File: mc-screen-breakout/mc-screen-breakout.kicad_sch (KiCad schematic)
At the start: 1 part, among them U1 E73-2G4M08S1C

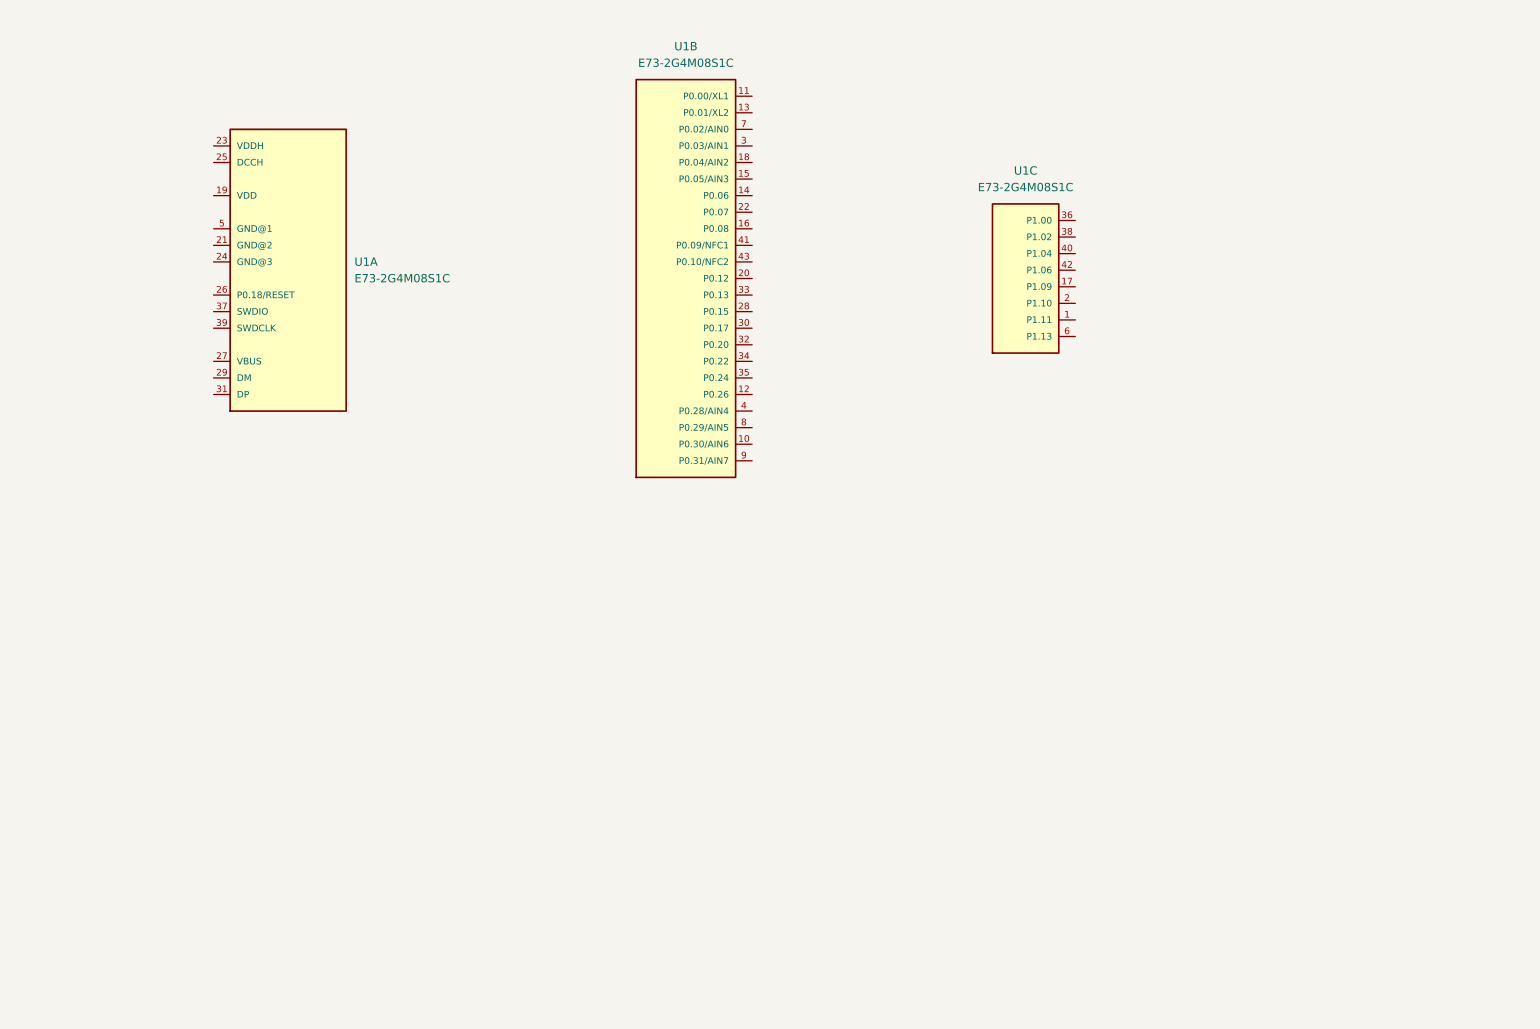
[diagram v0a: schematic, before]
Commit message: Initial microcontroller power on breakout
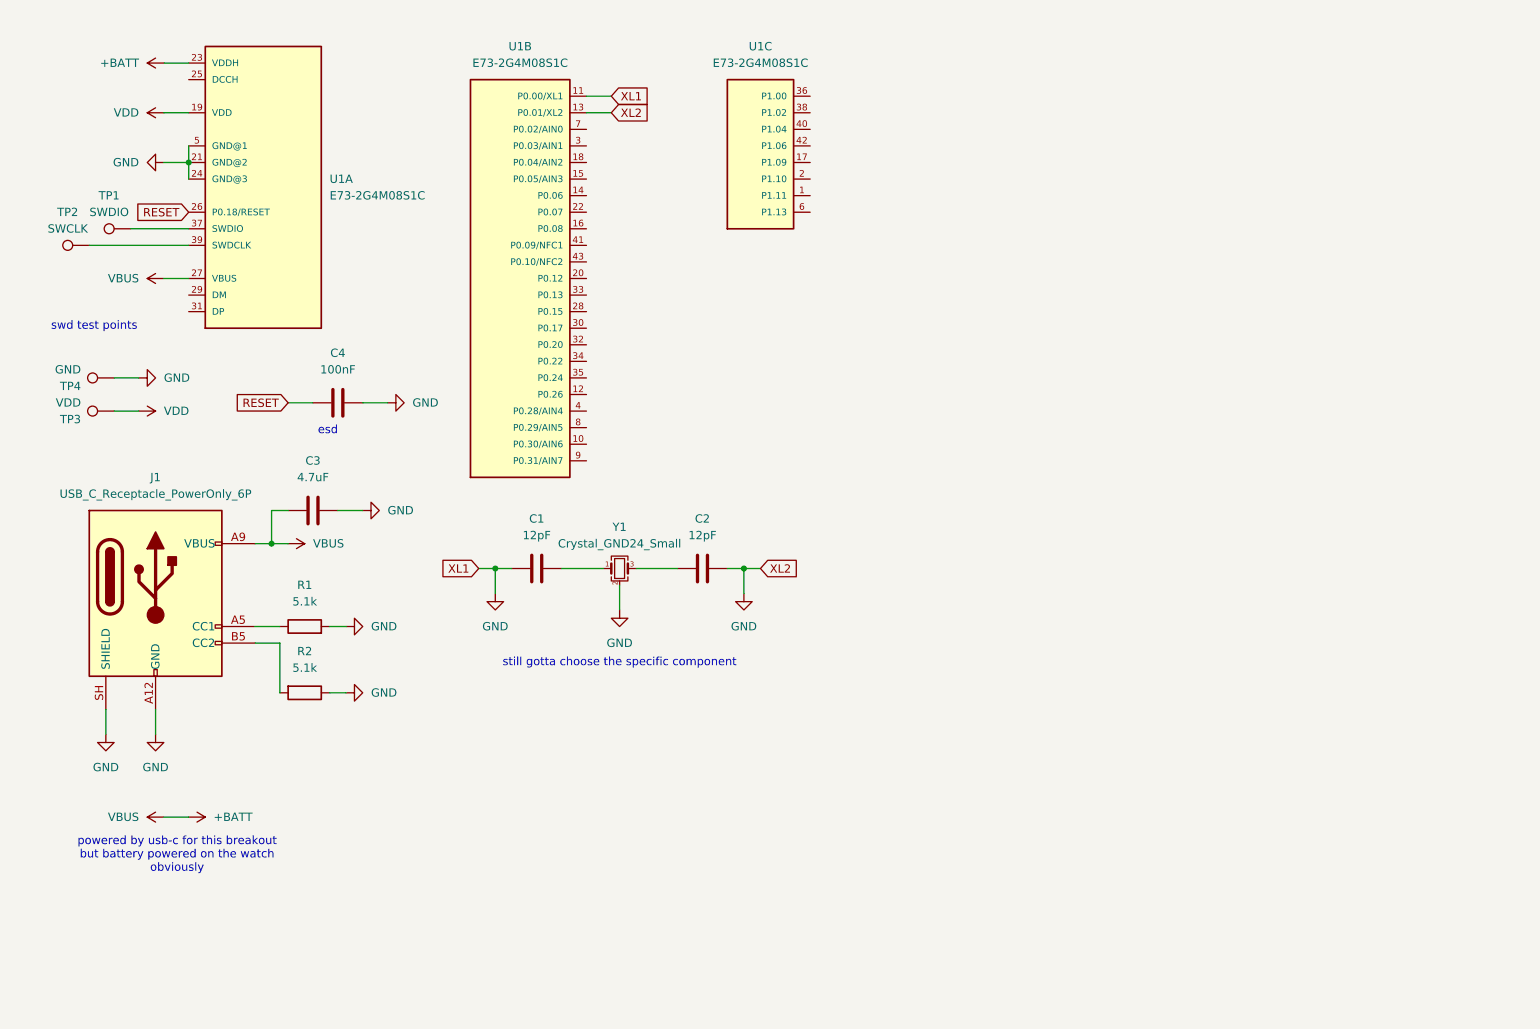
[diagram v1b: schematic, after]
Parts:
- added C1, C2: 12pF, symbol Device:C
- added C3: 4.7uF, symbol Device:C
- added C4: 100nF, symbol Device:C
- added J1: USB_C_Receptacle_PowerOnly_6P, symbol Connector:USB_C_Receptacle_PowerOnly_6P
- added R1, R2: 5.1k, symbol Device:R
- added TP1: SWDIO, symbol Connector:TestPoint
- added TP2: SWCLK, symbol Connector:TestPoint
- added TP3: VDD, symbol Connector:TestPoint
- added TP4: GND, symbol Connector:TestPoint
- added Y1: Crystal_GND24_Small, symbol Device:Crystal_GND24_Small
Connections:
- net GND: now reaches U1.11 (P0.00/XL1)
- net GND: now also U1.13 (P0.01/XL2), U1.21 (GND@2), U1.24 (GND@3), U1.5 (GND@1), C1.1, C2.2, C3.2, C4.2, J1.A12 (GND), J1.B12 (GND), J1.SH (SHIELD), R1.2, R2.1, TP4.1, Y1.2 (G), Y1.4 (G)
- net VDD: now reaches U1.19 (VDD)
- net VDD: now also TP3.1
- net +BATT: now reaches U1.23 (VDDH)
- net +BATT: now also U1.27 (VBUS), C3.1, J1.A9 (VBUS), J1.B9 (VBUS)
- net RESET: now reaches U1.26 (P0.18/RESET)
- net RESET: now also C4.1
- net at U1.37 (SWDIO): now also TP1.1
- net at U1.39 (SWDCLK): now also TP2.1
- new net: J1.A5 (CC1), R1.1
- new net: C1.2, Y1.1
- new net: C2.1, Y1.3
- new net: J1.B5 (CC2), R2.2
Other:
- note added: "esd"
- note added: "powered by usb-c for this breakout but battery powered on the watch obviously"
- note added: "still gotta choose the specific component"
- note added: "swd test points"
- moved on the sheet: U1A, U1B, U1C

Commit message: Switched to new Raytac module
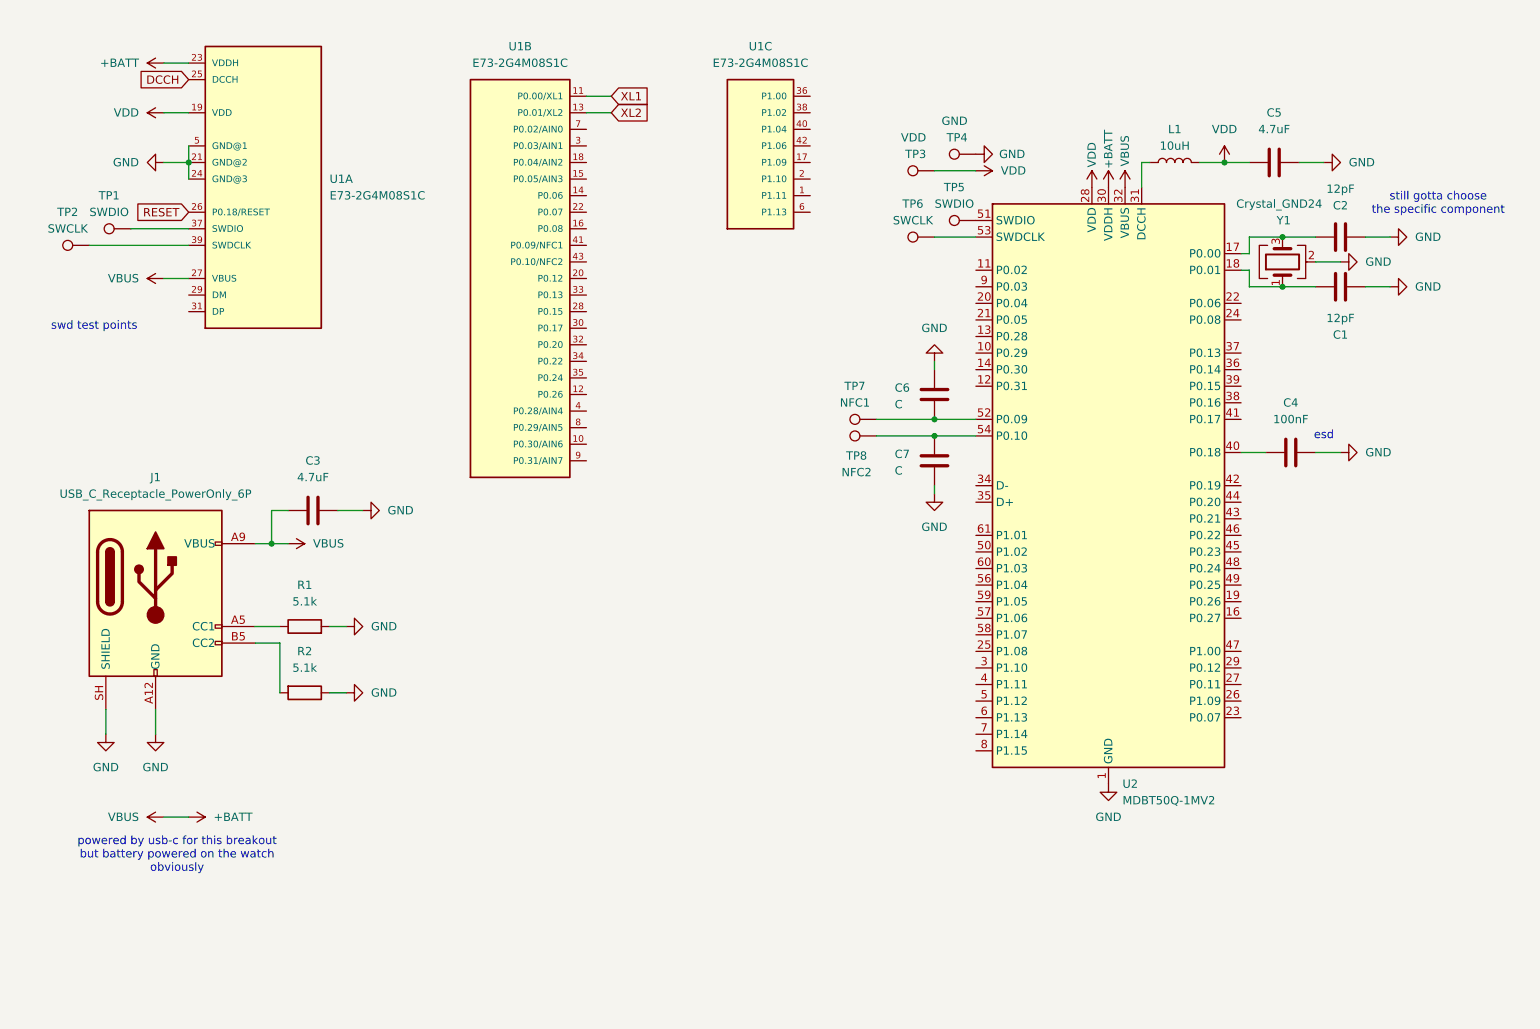
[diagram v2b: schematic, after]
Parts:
- removed Y1: Crystal_GND24_Small, symbol Device:Crystal_GND24_Small
- added C5: 4.7uF, symbol Device:C
- added C6, C7: C, symbol Device:C
- added L1: 10uH, symbol Device:L
- added TP5: SWDIO, symbol Connector:TestPoint
- added TP6: SWCLK, symbol Connector:TestPoint
- added TP7: NFC1, symbol Connector:TestPoint
- added TP8: NFC2, symbol Connector:TestPoint
- added U2: MDBT50Q-1MV2, RF_Module:Raytac_MDBT50Q, symbol RF_Module:MDBT50Q-1MV2
- added Y1: Crystal_GND24, symbol Device:Crystal_GND24
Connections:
- net +BATT: now also U2.30 (VDDH), U2.32 (VBUS)
- net GND: now also C5.2, C6.1, C7.2, U2.1 (GND), U2.15 (GND), U2.2 (GND), U2.33 (GND), U2.55 (GND), Y1.2 (G), Y1.4 (G); no longer U1.11 (P0.00/XL1), U1.13 (P0.01/XL2)
- net RESET: no longer C4.1
- net VDD: now also C5.1, L1.2, U2.28 (VDD)
- net at C1.2: now also U2.18 (P0.01), Y1.1
- net at C2.1: now also U2.17 (P0.00), Y1.3
- net DCCH: now reaches U1.25 (DCCH)
- new net: L1.1, U2.31 (DCCH)
- new net: C4.1, U2.40 (P0.18)
- new net: TP6.1, U2.53 (SWDCLK)
- new net: C7.1, TP8.1, U2.54 (P0.10)
- new net: C6.2, TP7.1, U2.52 (P0.09)
- new net: TP5.1, U2.51 (SWDIO)
- new net XL1: U1.11 (P0.00/XL1)
- new net XL2: U1.13 (P0.01/XL2)
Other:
- moved on the sheet: C4, TP3, TP4

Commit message: Added LCD FPC female connector
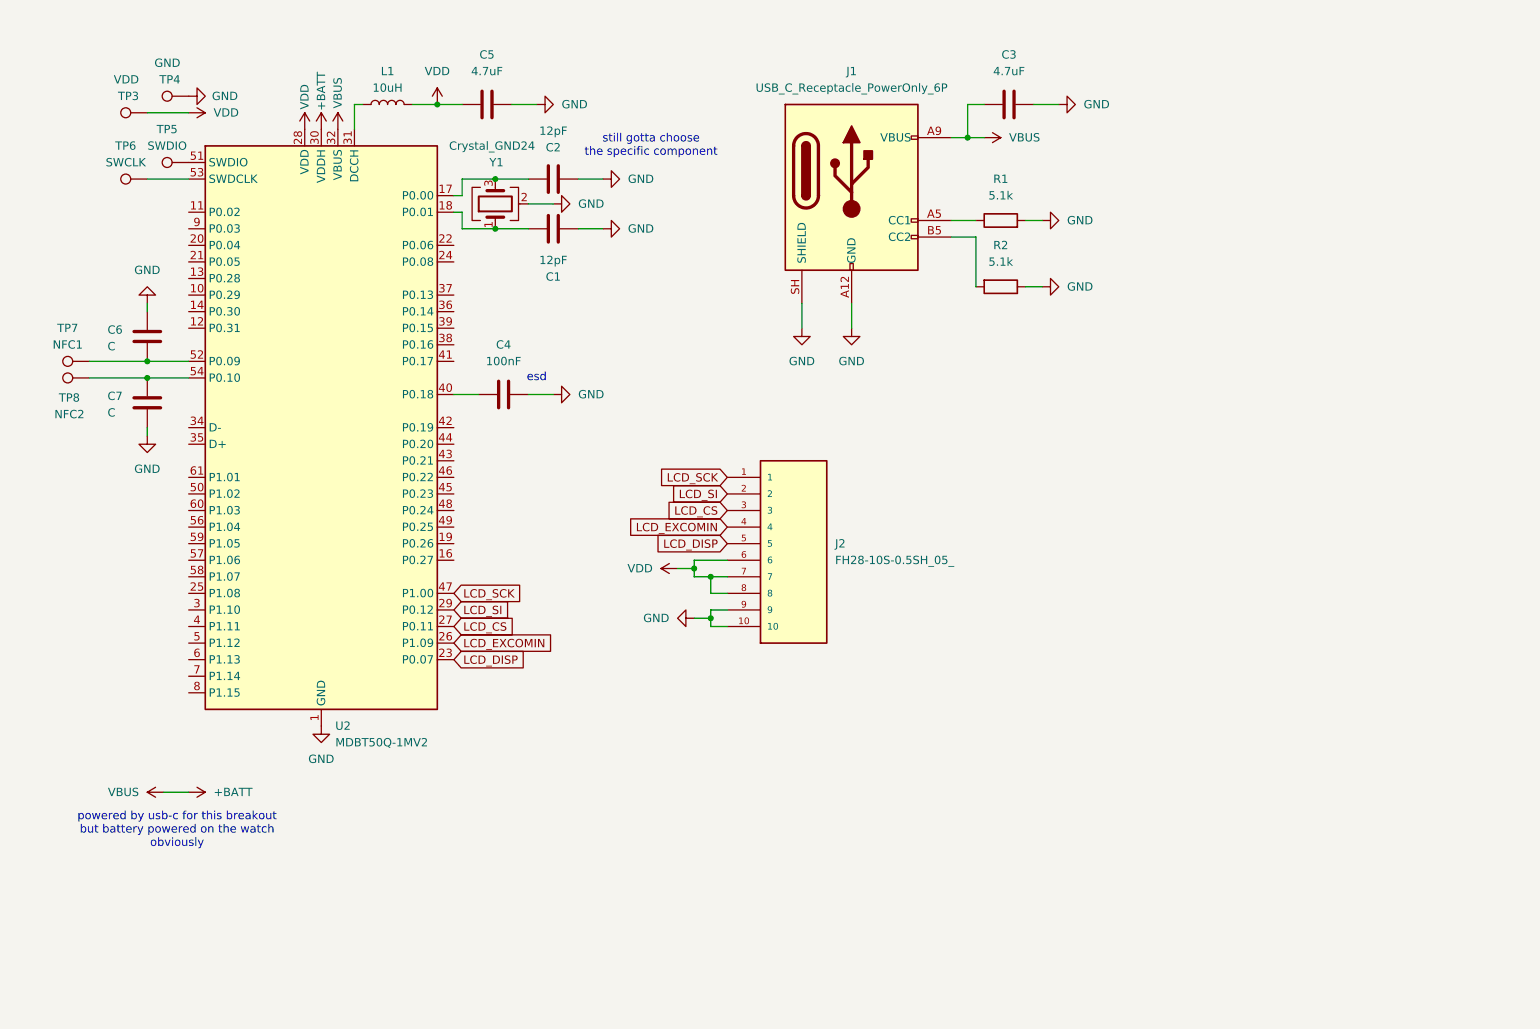
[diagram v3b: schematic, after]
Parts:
- removed TP1: SWDIO, symbol Connector:TestPoint
- removed TP2: SWCLK, symbol Connector:TestPoint
- removed U1: E73-2G4M08S1C, E73-2G4M08S1C:E73-2G4M08S1C, symbol E73-2G4M08S1C:E73-2G4M08S1C
- added J2: FH28-10S-0.5SH_05_, FH28-10S-0.5SH_05_:HIROSE_FH28-10S-0.5SH_05_, symbol FH28-10S-0.5SH_05_:FH28-10S-0.5SH_05_
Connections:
- net GND: now also J2.10, J2.9
- net VDD: now also J2.6, J2.7, J2.8
- net LCD_DISP: now reaches U2.23 (P0.07)
- net LCD_DISP: now also J2.5
- net LCD_EXCOMIN: now reaches U2.26 (P1.09)
- net LCD_EXCOMIN: now also J2.4
- net LCD_CS: now reaches U2.27 (P0.11)
- net LCD_CS: now also J2.3
- net LCD_SI: now reaches U2.29 (P0.12)
- net LCD_SI: now also J2.2
- net LCD_SCK: now reaches U2.47 (P1.00)
- net LCD_SCK: now also J2.1
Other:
- note removed: "swd test points"
- moved on the sheet: C1, C2, C3, C4, C5, C6, C7, J1, L1, R1, R2, TP3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

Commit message: Added missing decoupling caps
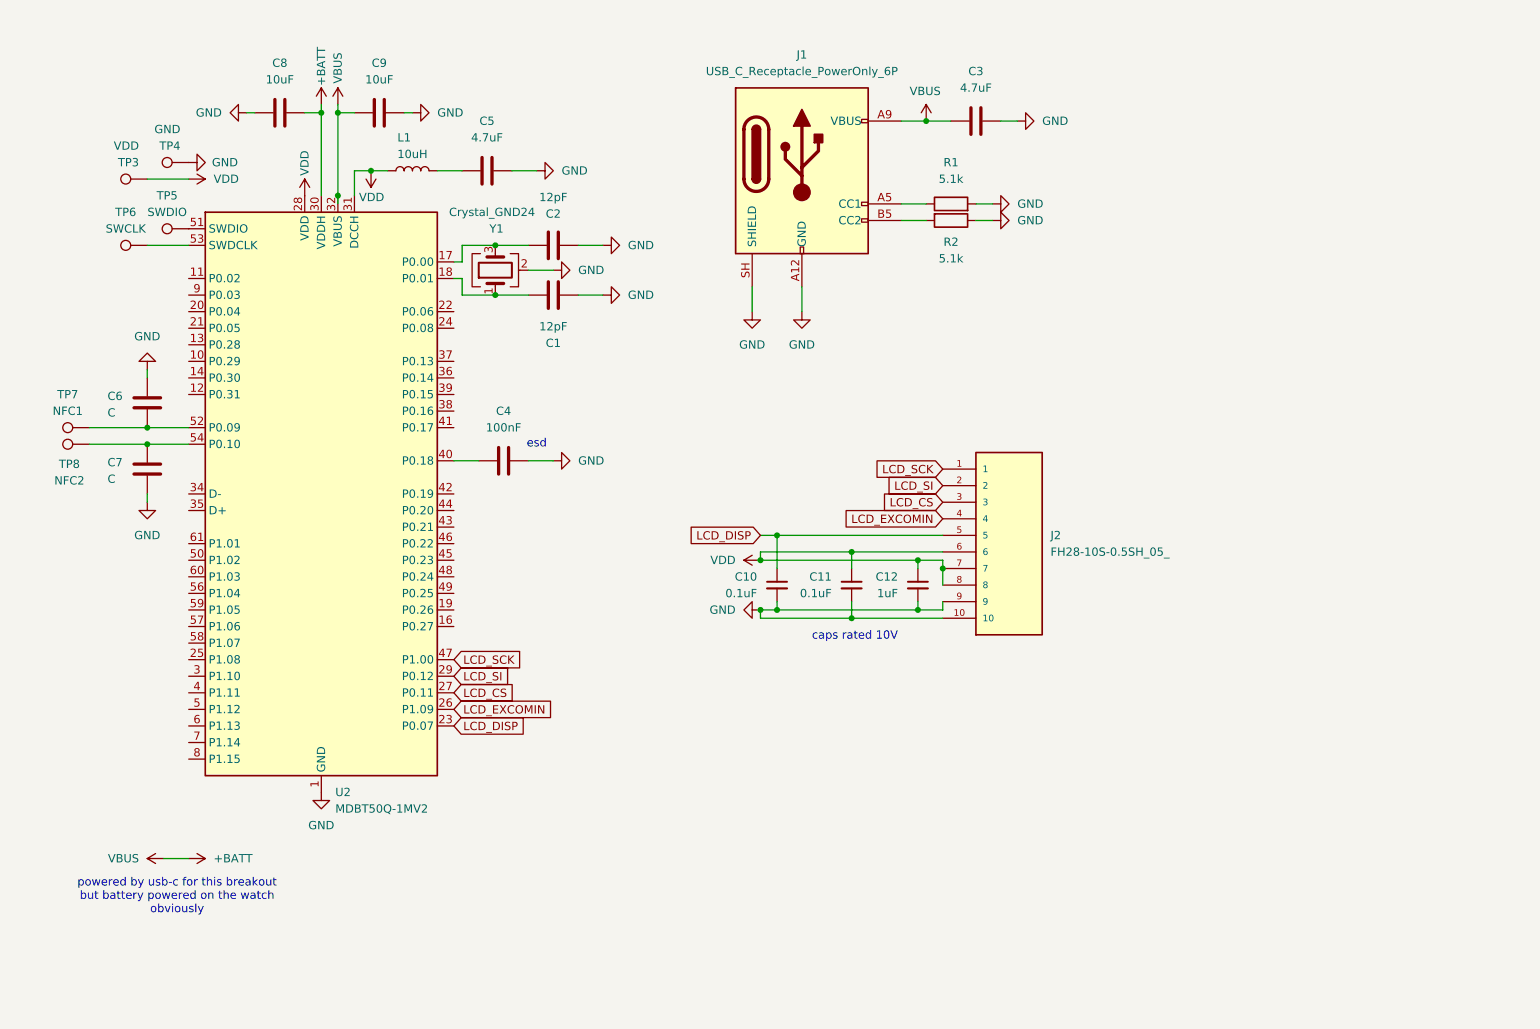
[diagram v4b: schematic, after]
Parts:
- added C10, C11: 0.1uF, symbol Device:C_Small
- added C12: 1uF, symbol Device:C_Small
- added C8, C9: 10uF, symbol Device:C
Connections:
- net +BATT: now also C8.1, C9.1
- net GND: now also C10.2, C11.2, C12.2, C8.2, C9.2
- net LCD_DISP: now also C10.1
- net VDD: now also L1.1, U2.31 (DCCH), C11.1, C12.1; no longer C5.1, L1.2
- new net: C5.1, L1.2
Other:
- note added: "caps rated 10V"
- note removed: "still gotta choose the specific component"
- moved on the sheet: C1, C2, C3, C4, C5, C6, C7, J1, J2, L1, R1, R2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
